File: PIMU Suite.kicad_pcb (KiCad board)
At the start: 2 copper layers, 77 x 50.5 mm, 16 parts, among them U2 MICROSD_SPI_OR_SDIO_CARD

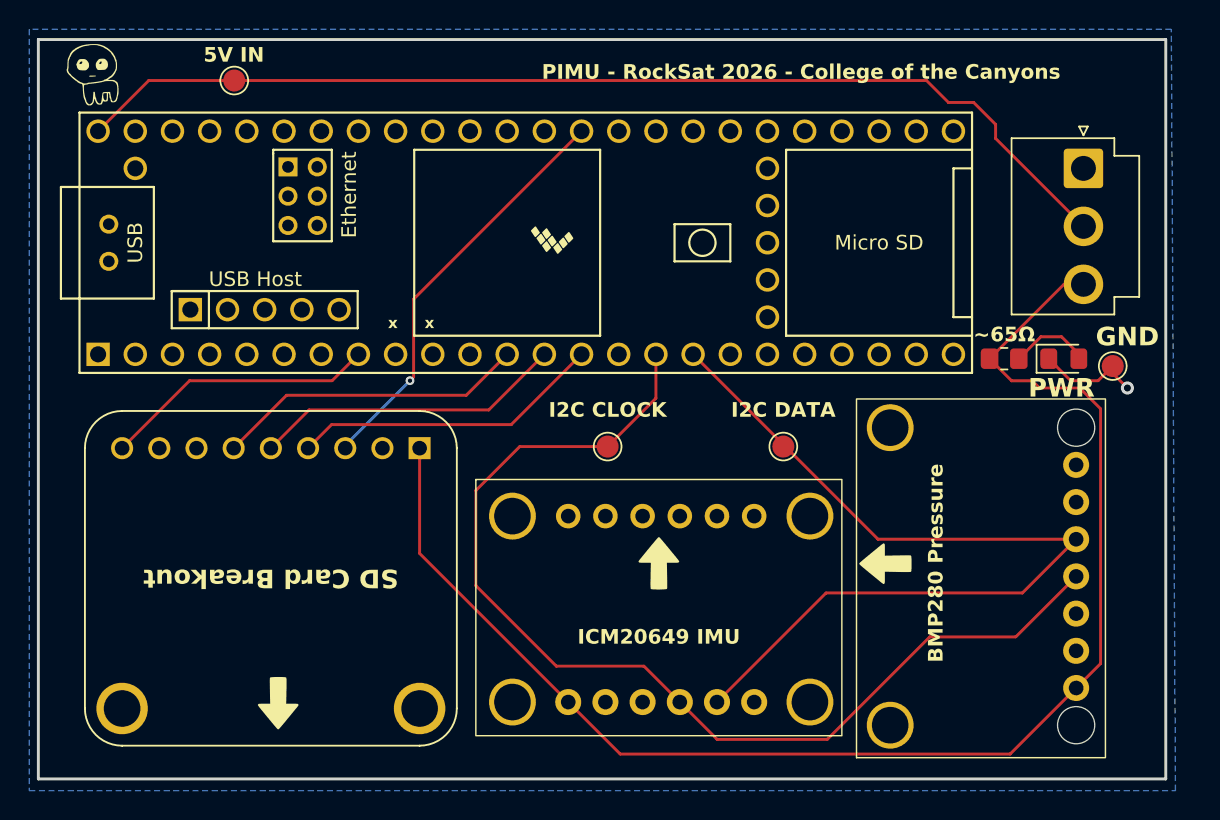
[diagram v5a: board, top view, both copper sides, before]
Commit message: Add TE line
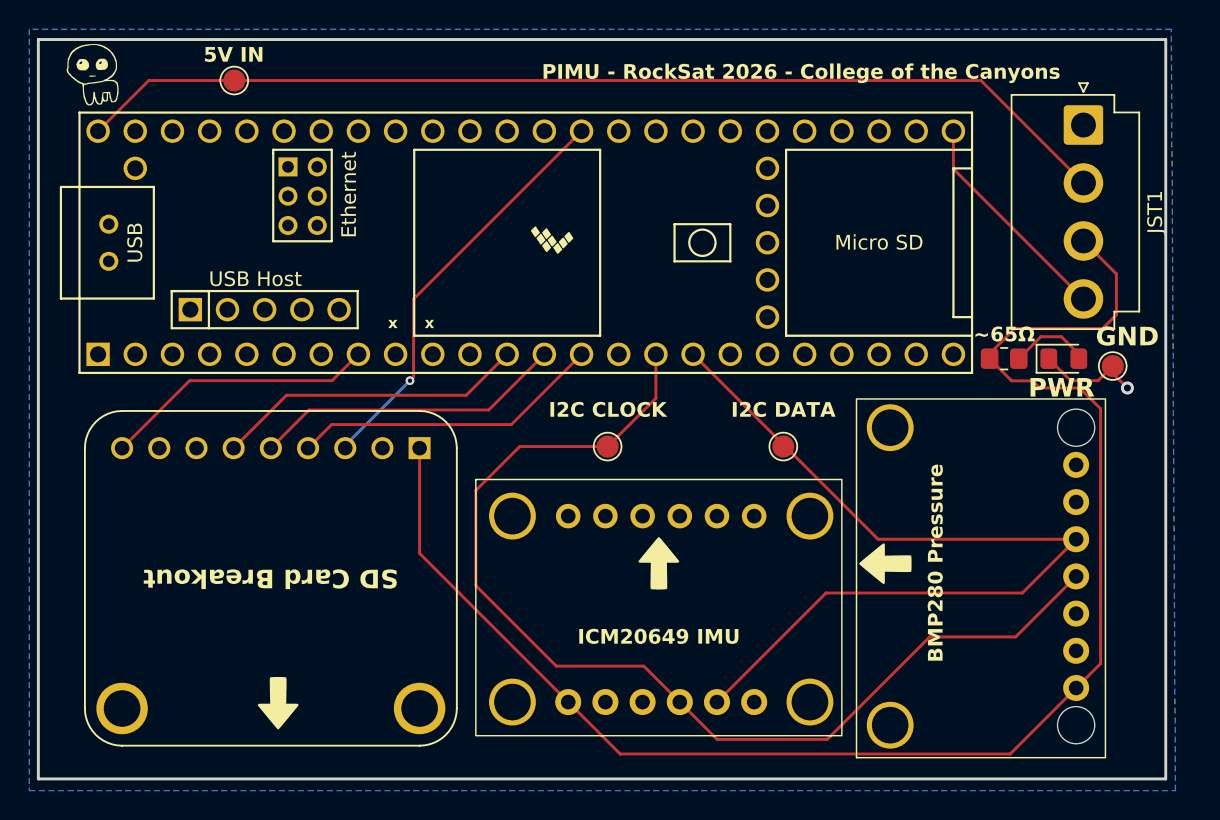
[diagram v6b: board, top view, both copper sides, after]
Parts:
- JST1: footprint Connector_JST:JST_VH_B3P-VH-B_1x03_P3.96mm_Vertical -> Connector_JST:JST_VH_B4P-VH-B_1x04_P3.96mm_Vertical
- moved JST1 2.96 mm to (177.5, 78.0)
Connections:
- TEENSY1 pad 25: unconnected-(TEENSY1-33_MCLK2-Pad25) -> /TE
- TEENSY1 pad 8: Net-(TEENSY1-6_OUT1D) -> unconnected-(TEENSY1-6_OUT1D-Pad8)
- U2 pad 9: Net-(TEENSY1-6_OUT1D) -> unconnected-(U2-DET-Pad9)
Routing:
- net Net-(TEENSY1-6_OUT1D): track 18.8 -> 0.00 mm
- net (no net): track 0.00 -> 18.8 mm
- net /TE: track 0.00 -> 15.1 mm
- net +3.3V: track 97.0 -> 104.5 mm
- net +5V: track 73.4 -> 71.6 mm

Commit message: Rename value
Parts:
- JST1: value S4B-XH-A-1 -> JST
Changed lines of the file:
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@@
 		(tags "connector JST VH vertical")
 		(property "Reference" "JST1"
-			(at 5.94 -4.9 270)
-			(layer "F.SilkS")
-			(effects
-				(font
-					(size 1 1)
-					(thickness 0.15)
-				)
-			)
-		)
-		(property "Value" "S4B-XH-A-1"
-			(at 5.94 6 270)
+			(at 5.94 -4.9 90)
+			(layer "F.SilkS")
+			(effects
+				(font
+					(size 1 1)
+					(thickness 0.15)
+				)
+			)
+		)
+		(property "Value" "JST"
+			(at 5.94 6 90)
 			(layer "F.Fab")
 			(effects
@@
 		)
 		(property "Datasheet" "~"
-			(at 0 0 270)
+			(at 0 0 90)
 			(layer "F.Fab")
 			(hide yes)
@@
 		)
 		(property "Description" "Generic connector, single row, 01x04, script generated"
-			(at 0 0 270)
+			(at 0 0 90)
 			(layer "F.Fab")
 			(hide yes)
@@
 		)
 		(fp_text user "${REFERENCE}"
-			(at 5.94 4.1 270)
-			(layer "F.Fab")
-			(effects
+			(at 5.94 4.1 90)
+			(layer "F.Fab")
+			(effects

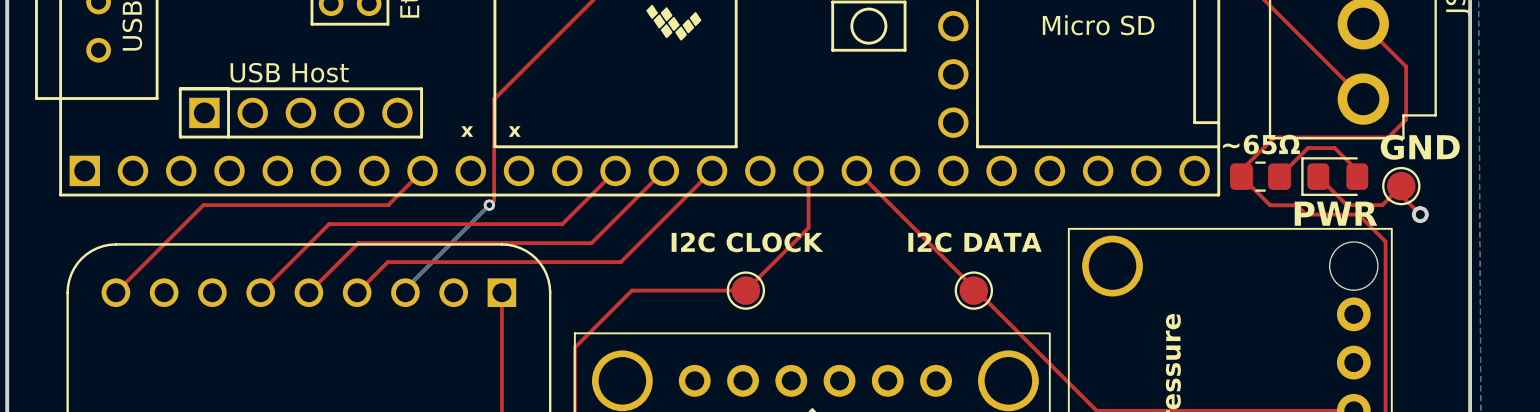
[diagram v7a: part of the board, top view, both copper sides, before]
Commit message: PCBWay Limitations
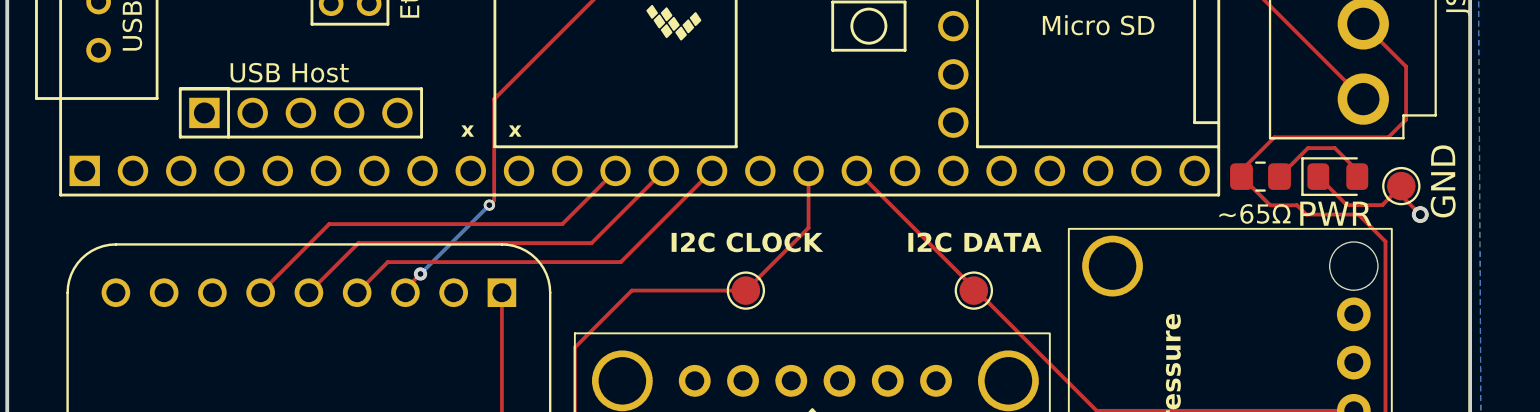
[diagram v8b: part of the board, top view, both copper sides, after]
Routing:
- net (no net): track 18.8 -> 0.00 mm
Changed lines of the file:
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@@
 	(generator_version "9.0")
 	(general
-		(thickness 1.6)
+		(thickness 1.600198)
 		(legacy_teardrops no)
 	)
@@
 	)
 	(layers
-		(0 "F.Cu" jumper)
-		(2 "B.Cu" signal)
-		(9 "F.Adhes" user "F.Adhesive")
-		(11 "B.Adhes" user "B.Adhesive")
+		(0 "F.Cu" signal "Front")
+		(2 "B.Cu" signal "Back")
 		(13 "F.Paste" user)
 		(15 "B.Paste" user)
@@
 		(1 "F.Mask" user)
 		(3 "B.Mask" user)
-		(17 "Dwgs.User" user "User.Drawings")
-		(19 "Cmts.User" user "User.Comments")
-		(21 "Eco1.User" user "User.Eco1")
-		(23 "Eco2.User" user "User.Eco2")
 		(25 "Edge.Cuts" user)
 		(27 "Margin" user)
@@
 		(29 "B.CrtYd" user "B.Courtyard")
 		(35 "F.Fab" user)
-		(33 "B.Fab" user)
-		(39 "User.1" user)
-		(41 "User.2" user)
-		(43 "User.3" user)
-		(45 "User.4" user)
 	)
 	(setup
@@
 			(layer "dielectric 1"
 				(type "core")
-				(thickness 1.51)
+				(thickness 1.510198)
 				(material "FR4")
 				(epsilon_r 4.5)
@@
 			(layer "F.SilkS")
 		)
-		(fp_line
-			(start -2.45 5.3)
-			(end 14.33 5.3)
-			(stroke
-				(width 0.05)
-				(type solid)
-			)
-			(layer "F.CrtYd")
-		)
-		(fp_line
-			(start 14.33 5.3)
-			(end 14.33 -4.2)
-			(stroke
-				(width 0.05)
-				(type solid)
-			)
-			(layer "F.CrtYd")
-		)
-		(fp_line
+		(fp_rect
 			(start -2.45 -4.2)
-			(end -2.45 5.3)
-			(stroke
-				(width 0.05)
-				(type solid)
-			)
-			(layer "F.CrtYd")
-		)
-		(fp_line
-			(start 14.33 -4.2)
-			(end -2.45 -4.2)
+			(end 14.33 5.3)
 			(stroke
 				(width 0.05)
 				(type solid)
 			)
+			(fill no)
 			(layer "F.CrtYd")
 		)
 		(fp_line
-			(start -1.95 4.8)
-			(end 13.83 4.8)
-			(stroke
-				(width 0.1)
-				(type solid)
-			)
-			(layer "F.Fab")
-		)
-		(fp_line
-			(start 13.83 4.8)
-			(end 13.83 -2)
-			(stroke
-				(width 0.1)
-				(type solid)
-			)
-			(layer "F.Fab")
-		)
-		(fp_line
 			(start -1.95 1)
 			(end -0.95 0)
@@
 		)
 		(fp_line
-			(start -1.95 -2)
-			(end -1.95 4.8)
-			(stroke
-				(width 0.1)
-				(type solid)
-			)
-			(layer "F.Fab")
-		)
-		(fp_line
 			(start -0.75 -2)
 			(end -0.75 -3.7)
@@
 		)
 		(fp_line
-			(start 13.83 -2)
-			(end -1.95 -2)
+			(start -0.75 -3.7)
+			(end 12.63 -3.7)
 			(stroke
 				(width 0.1)
@@
 		)
 		(fp_line
-			(start -0.75 -3.7)
-			(end 12.63 -3.7)
+			(start 12.63 -3.7)
+			(end 12.63 -2)
 			(stroke
 				(width 0.1)
@@
 			(layer "F.Fab")
 		)
-		(fp_line
-			(start 12.63 -3.7)
-			(end 12.63 -2)
+		(fp_rect
+			(start -1.95 -2)
+			(end 13.83 4.8)
 			(stroke
 				(width 0.1)
 				(type solid)
 			)
+			(fill no)
 			(layer "F.Fab")
 		)
@@
 				(font
 					(size 1.27 1.27)
-					(thickness 0.254)
-					(bold yes)
+					(thickness 0.15875)
 				)
 			)
@@
 			(layer "F.SilkS")
 		)
-		(fp_line
+		(fp_rect
 			(start -1.85 -0.95)
-			(end 1.85 -0.95)
-			(stroke
-				(width 0.05)
-				(type solid)
-			)
-			(layer "F.CrtYd")
-		)
-		(fp_line
-			(start -1.85 0.95)
-			(end -1.85 -0.95)
-			(stroke
-				(width 0.05)
-				(type solid)
-			)
-			(layer "F.CrtYd")
-		)
-		(fp_line
-			(start 1.85 -0.95)
 			(end 1.85 0.95)
 			(stroke
@@
 				(type solid)
 			)
-			(layer "F.CrtYd")
-		)
-		(fp_line
-			(start 1.85 0.95)
-			(end -1.85 0.95)
-			(stroke
-				(width 0.05)
-				(type solid)
-			)
+			(fill no)
 			(layer "F.CrtYd")
 		)
@@
 		)
 		(property "Description" "GND"
-			(at 1 -2 0)
+			(at 2.25 -0.25 90)
 			(unlocked yes)
 			(layer "F.SilkS")
@@
 				(font
 					(size 1.27 1.27)
-					(thickness 0.254)
-					(bold yes)
+					(thickness 0.15875)
 				)
 			)
@@
 		)
 		(property "Value" "~65Ω"
-			(at 0 1.65 180)
+			(at 0.3375 -2 180)
 			(layer "F.SilkS")
 			(effects
 				(font
 					(size 1 1)
-					(thickness 0.2)
-					(bold yes)
+					(thickness 0.125)
 				)
 			)
@@
 			(layer "F.SilkS")
 		)
-		(fp_line
-			(start 1.85 0.95)
-			(end -1.85 0.95)
-			(stroke
-				(width 0.05)
-				(type solid)
-			)
-			(layer "F.CrtYd")
-		)
-		(fp_line
-			(start 1.85 -0.95)
-			(end 1.85 0.95)
-			(stroke
-				(width 0.05)
-				(type solid)
-			)
-			(layer "F.CrtYd")
-		)
-		(fp_line
-			(start -1.85 0.95)
-			(end -1.85 -0.95)
-			(stroke
-				(width 0.05)
-				(type solid)
-			)
-			(layer "F.CrtYd")
-		)
-		(fp_line
+		(fp_rect
 			(start -1.85 -0.95)
-			(end 1.85 -0.95)
+			(end 1.85 0.95)
 			(stroke
 				(width 0.05)
 				(type solid)
 			)
+			(fill no)
 			(layer "F.CrtYd")
 		)
-		(fp_line
-			(start 1 0.625)
-			(end -1 0.625)
-			(stroke
-				(width 0.1)
-				(type solid)
-			)
-			(layer "F.Fab")
-		)
-		(fp_line
-			(start 1 -0.625)
-			(end 1 0.625)
-			(stroke
-				(width 0.1)
-				(type solid)
-			)
-			(layer "F.Fab")
-		)
-		(fp_line
-			(start -1 0.625)
-			(end -1 -0.625)
-			(stroke
-				(width 0.1)
-				(type solid)
-			)
-			(layer "F.Fab")
-		)
-		(fp_line
+		(fp_rect
 			(start -1 -0.625)
-			(end 1 -0.625)
+			(end 1 0.625)
 			(stroke
 				(width 0.1)
 				(type solid)
 			)
+			(fill no)
 			(layer "F.Fab")
 		)
@@
 		(effects
 			(font
-				(size 0.75 0.75)
+				(size 0.8 0.8)
 				(thickness 0.1875)
 				(bold yes)
@@
 		(effects
 			(font
-				(size 0.75 0.75)
+				(size 0.8 0.8)
 				(thickness 0.1875)
 				(bold yes)
@@
 	)
 	(segment
-		(start 116.45 95.5)
-		(end 126.18 95.5)
-		(width 0.2)
-		(layer "F.Cu")
-		(net 0)
-	)
-	(segment
-		(start 111.84 100.11)
-		(end 116.45 95.5)
-		(width 0.2)
-		(layer "F.Cu")
-		(net 0)
-	)
-	(segment
-		(start 126.18 95.5)
-		(end 127.98 93.7)
-		(width 0.2)
-		(layer "F.Cu")
-		(net 0)
-	)
-	(segment
 		(start 135.34 96.5)
 		(end 138.14 93.7)
@@
 	)
 	(segment
+		(start 127.08 100.11)
+		(end 127.08 99.92)
+		(width 0.2)
+		(layer "F.Cu")
+		(net 19)
+	)
+	(segment
 		(start 131.5 95.5)
 		(end 131.75 95.25)
@@
 	)
 	(segment
+		(start 127.08 99.92)
+		(end 127.875 99.125)
+		(width 0.2)
+		(layer "F.Cu")
+		(net 19)
+	)
+	(segment
 		(start 131.75 95.25)
 		(end 131.75 89.93)
@@
 	)
 	(via
-		(at 131.5 95.5)
-		(size 0.6)
+		(at 127.875 99.125)
+		(size 0.7)
 		(drill 0.3)
 		(layers "F.Cu" "B.Cu")
@@
 	)
 	(via
-		(at 127.08 100.11)
+		(at 131.5 95.5)
 		(size 0.6)
 		(drill 0.3)
@@
 	)
 	(segment
-		(start 127.08 99.92)
+		(start 127.875 99.125)
 		(end 131.5 95.5)
 		(width 0.2)
